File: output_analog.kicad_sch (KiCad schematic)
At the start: 48 parts, among them Q1 DMTH10H009LPSQ-13, Q2 BSR14, Q3 PMN280ENEA, U1 74LVC1G17, U2 TSV732IS, U3 TSV732IS

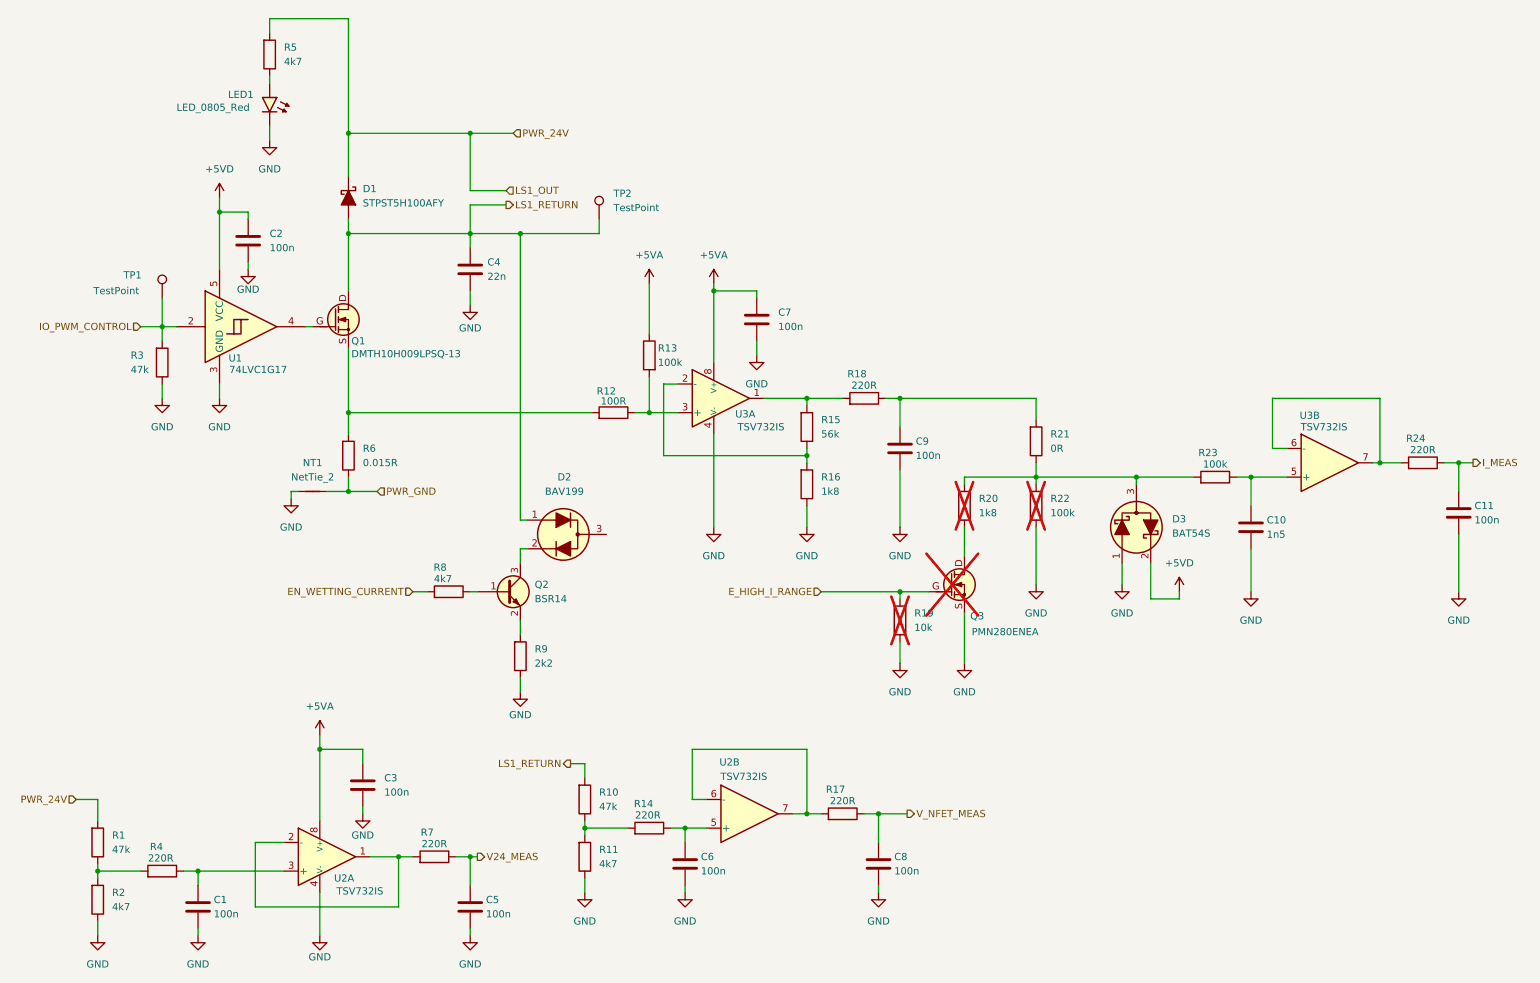
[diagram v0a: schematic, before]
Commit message: - Removed I2C lines - Added mission resistor between buffer and transistor gate - Removed wetting current & high range enable - Added ILI9341 TFT LCD - Removed OLED - Upped current gain to ~100
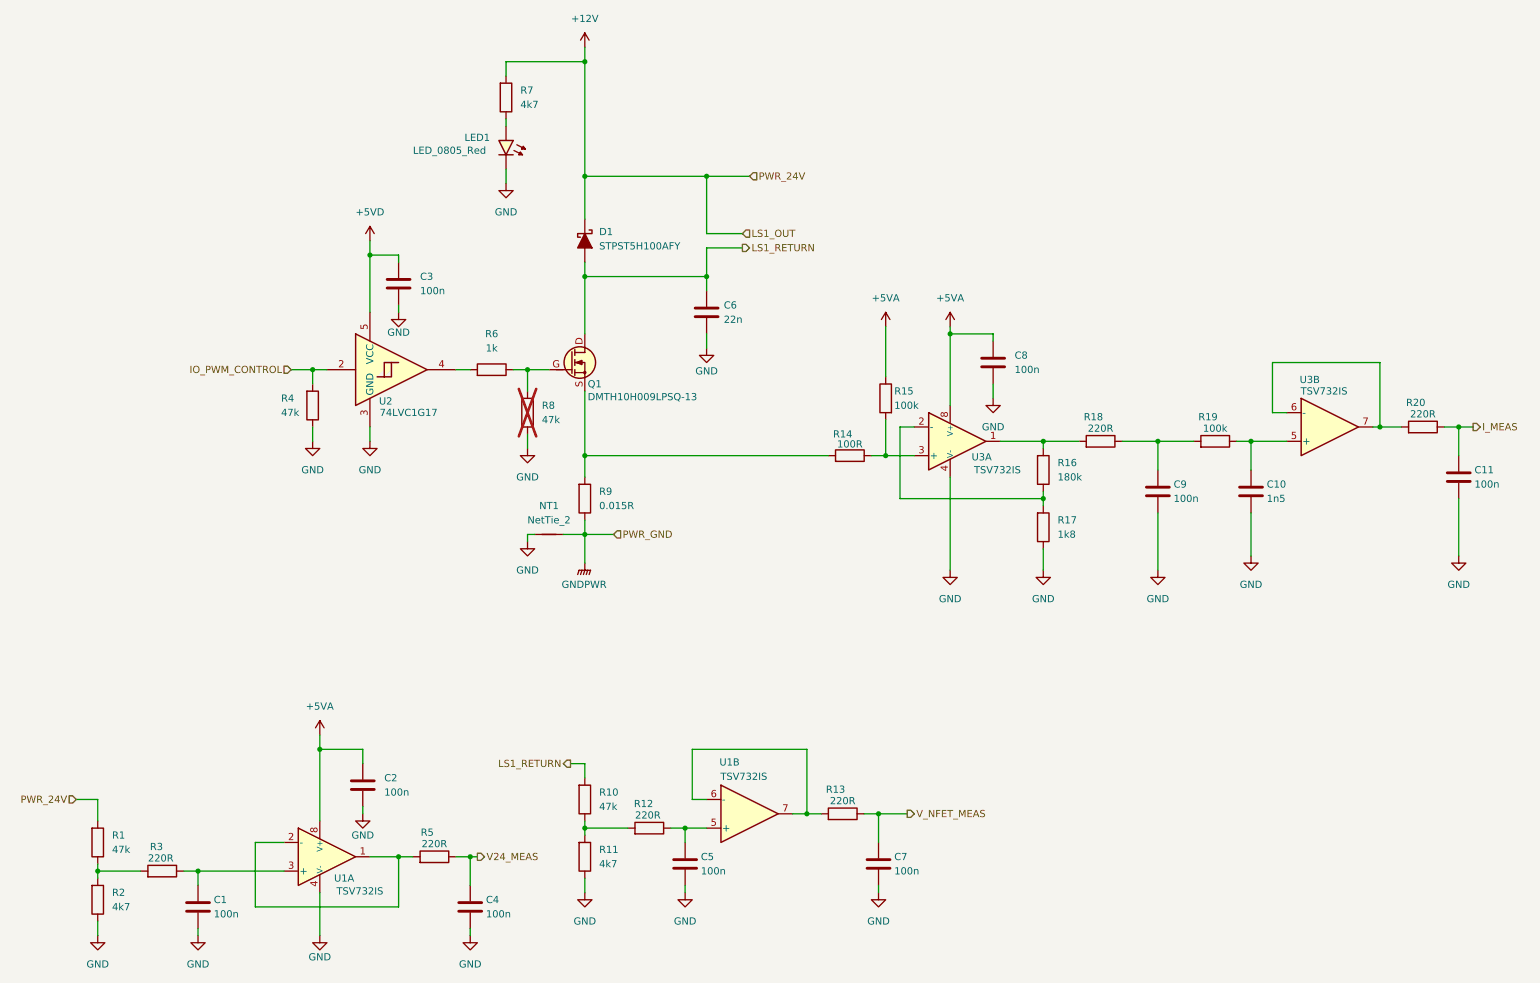
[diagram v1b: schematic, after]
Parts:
- removed D2: BAV199, PCM_Package_TO_SOT_SMD_AKL:SOT-23, symbol PCM_Diode_AKL:BAV199
- removed D3: BAT54S, PCM_Package_TO_SOT_SMD_AKL:SOT-23, symbol PCM_Diode_Schottky_AKL:BAT54S
- removed Q2: BSR14, PCM_Package_TO_SOT_SMD_AKL:SOT-23, symbol PCM_Transistor_BJT_AKL:BSR14
- removed Q3: PMN280ENEA, athanniss-semiconductors:SC-74-6_1.5x2.9mm_P0.95mm, symbol athanniss-lib:PMN280ENEA
- removed R19: 10k, PCM_Resistor_SMD_AKL:R_0603_1608Metric, symbol PCM_Resistor_AKL:R_0603
- removed R20: 1k8, PCM_Resistor_SMD_AKL:R_0603_1608Metric, symbol PCM_Resistor_AKL:R_0603
- removed R21: 0R, PCM_Resistor_SMD_AKL:R_0603_1608Metric, symbol PCM_Resistor_AKL:R_0603
- removed R22: 100k, PCM_Resistor_SMD_AKL:R_0603_1608Metric, symbol PCM_Resistor_AKL:R_0603
- removed R9: 2k2, PCM_Resistor_SMD_AKL:R_0603_1608Metric, symbol PCM_Resistor_AKL:R_0603
- removed TP1, TP2: TestPoint, TestPoint:TestPoint_THTPad_D1.0mm_Drill0.5mm, symbol Connector:TestPoint
- added R6: 1k, PCM_Resistor_SMD_AKL:R_0603_1608Metric, symbol PCM_Resistor_AKL:R_0603
- R16: renamed from R15; value 56k -> 180k
- R8: value 4k7 -> 47k; now not fitted
- renumbered C3 to C2, C2 to C3, C5 to C4, C6 to C5, C4 to C6, C8 to C7, C7 to C8, R14 to R12, R17 to R13, R12 to R14, R13 to R15, R16 to R17, R23 to R19, R24 to R20, R4 to R3, R3 to R4, R7 to R5, R5 to R7, R6 to R9, U2 to U1, U1 to U2
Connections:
- net EN_WETTING_CURRENT is gone; now on net GND: R8.1
- net at R19.1: now also C9.1, R18.2
- net at R8.2: now also Q1.G, R6.2
- net at U2.4: now also R6.1; no longer Q1.G
- net LS1_OUT renamed +12V
- net PWR_GND renamed GNDPWR
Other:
- moved on the sheet: C10, C11, C3, C6, C8, C9, D1, LED1, NT1, Q1, R14, R15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
